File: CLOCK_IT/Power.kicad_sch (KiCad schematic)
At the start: 50 parts, among them Q1 AO3400A, Q2 AO3400A, SW1 CK_KMS2xxG, U10 DS1307ZN_, U4 AXP2101, U5 MC-264, Y2 ABS07-32.768KHZ-T

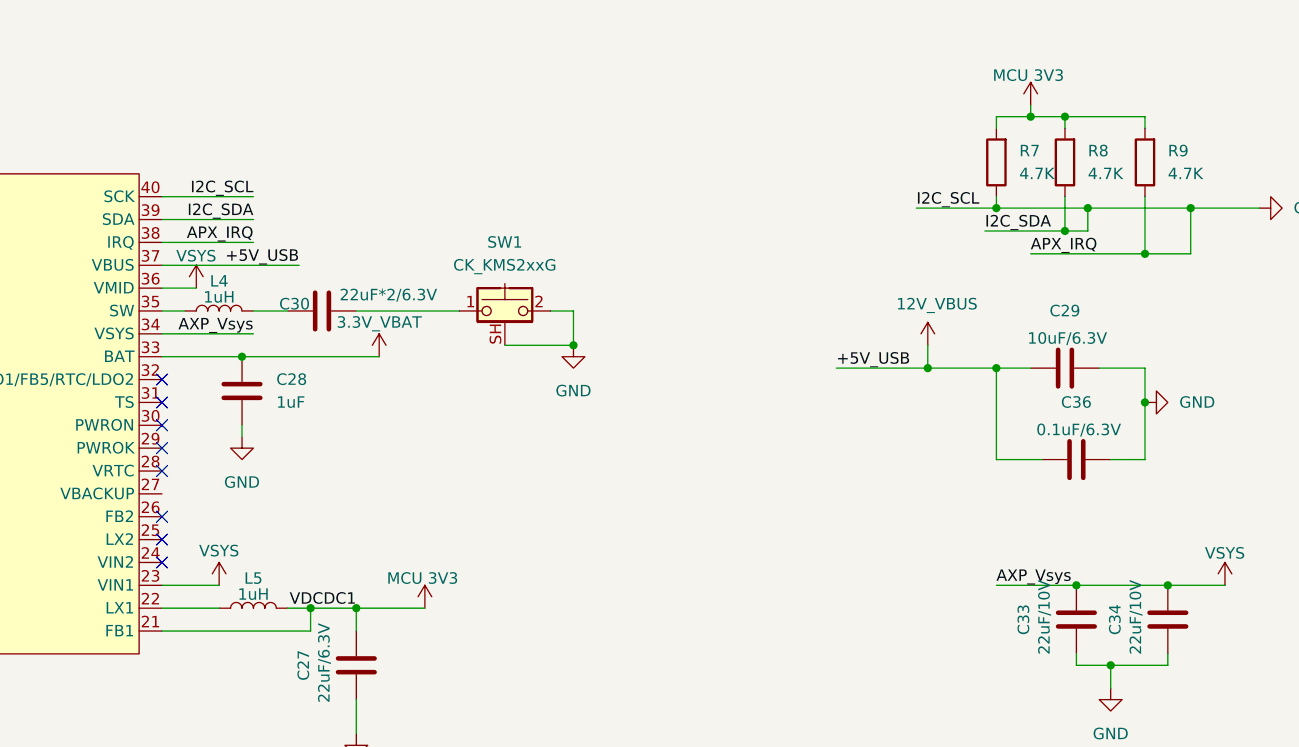
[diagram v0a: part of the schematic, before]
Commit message: :art: small Rereading errors for axp21010 Part 2
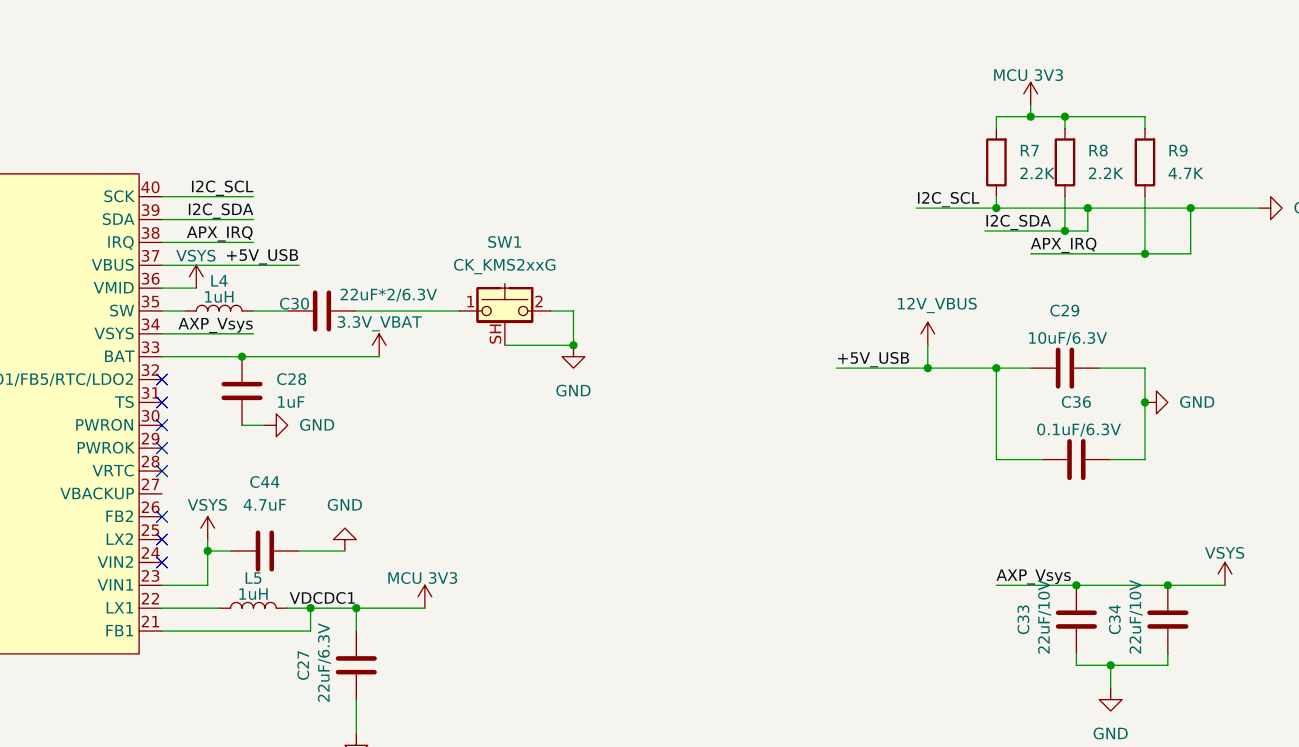
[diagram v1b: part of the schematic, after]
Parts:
- added C44: 4.7uF, symbol Device:C
- R7, R8: value 4.7K -> 2.2K
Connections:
- net GND: now also C44.2
- net VSYS: now also C44.1
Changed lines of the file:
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@@
 	)
 	(junction
+		(at 201.93 78.74)
+		(diameter 0)
+		(color 0 0 0 0)
+	)
+	(junction
 		(at 289.56 58.42)
 		(diameter 0)
@@
 	(wire
 		(pts
+			(xy 201.93 77.47) (xy 201.93 78.74)
+		)
+		(stroke
+			(width 0)
+			(type default)
+		)
+	)
+	(wire
+		(pts
 			(xy 115.57 201.93) (xy 120.65 201.93)
 		)
@@
 	(wire
 		(pts
-			(xy 205.74 64.77) (xy 205.74 66.04)
+			(xy 234.95 55.88) (xy 242.57 55.88)
 		)
 		(stroke
@@
 	(wire
 		(pts
-			(xy 234.95 55.88) (xy 242.57 55.88)
+			(xy 306.07 62.23) (xy 306.07 58.42)
 		)
 		(stroke
@@
 	(wire
 		(pts
-			(xy 306.07 62.23) (xy 306.07 58.42)
+			(xy 124.46 87.63) (xy 133.35 87.63)
 		)
 		(stroke
@@
 	(wire
 		(pts
-			(xy 124.46 87.63) (xy 133.35 87.63)
+			(xy 121.92 52.07) (xy 135.89 52.07)
 		)
 		(stroke
@@
 	(wire
 		(pts
-			(xy 121.92 52.07) (xy 135.89 52.07)
+			(xy 134.62 49.53) (xy 138.43 49.53)
 		)
 		(stroke
@@
 	(wire
 		(pts
-			(xy 134.62 49.53) (xy 138.43 49.53)
+			(xy 201.93 78.74) (xy 204.47 78.74)
 		)
 		(stroke
@@
 	(wire
 		(pts
+			(xy 201.93 78.74) (xy 201.93 82.55)
+		)
+		(stroke
+			(width 0)
+			(type default)
+		)
+	)
+	(wire
+		(pts
 			(xy 138.43 44.45) (xy 120.65 44.45)
 		)
@@
 	(wire
 		(pts
+			(xy 212.09 78.74) (xy 217.17 78.74)
+		)
+		(stroke
+			(width 0)
+			(type default)
+		)
+	)
+	(wire
+		(pts
 			(xy 119.38 38.1) (xy 119.38 35.56)
 		)
@@
 	(wire
 		(pts
+			(xy 208.28 64.77) (xy 205.74 64.77)
+		)
+		(stroke
+			(width 0)
+			(type default)
+		)
+	)
+	(wire
+		(pts
 			(xy 288.29 43.18) (xy 297.18 43.18)
 		)
@@
 	(wire
 		(pts
+			(xy 201.93 82.55) (xy 196.85 82.55)
+		)
+		(stroke
+			(width 0)
+			(type default)
+		)
+	)
+	(wire
+		(pts
 			(xy 35.56 40.64) (xy 35.56 45.72)
 		)
@@
 	(wire
 		(pts
-			(xy 196.85 82.55) (xy 203.2 82.55)
-		)
-		(stroke
-			(width 0)
-			(type default)
-		)
-	)
-	(wire
-		(pts
 			(xy 289.56 68.58) (xy 289.56 58.42)
 		)
@@
 	(symbol
 		(lib_id "power:GND")
-		(at 205.74 66.04 0)
+		(at 208.28 64.77 90)
 		(unit 1)
 		(exclude_from_sim no)
@@
 		(fields_autoplaced yes)
 		(property "Reference" "#PWR071"
-			(at 205.74 72.39 0)
+			(at 214.63 64.77 0)
 			(effects
 				(font
@@
 		)
 		(property "Value" "GND"
-			(at 205.74 71.12 0)
+			(at 212.09 64.7699 90)
 			(effects
 				(font
 					(size 1.27 1.27)
 				)
+				(justify right)
 			)
 		)
 		(property "Footprint" ""
-			(at 205.74 66.04 0)
+			(at 208.28 64.77 0)
 			(effects
 				(font
@@
 		)
 		(property "Datasheet" ""
-			(at 205.74 66.04 0)
+			(at 208.28 64.77 0)
 			(effects
 				(font
@@
 		)
 		(property "Description" "Power symbol creates a global label with name \"GND\" , ground"
-			(at 205.74 66.04 0)
+			(at 208.28 64.77 0)
 			(effects
 				(font
@@
 	(symbol
 		(lib_id "power:+3.3V")
-		(at 203.2 82.55 0)
+		(at 201.93 77.47 0)
 		(unit 1)
 		(exclude_from_sim no)
@@
 		(dnp no)
 		(property "Reference" "#PWR047"
-			(at 203.2 86.36 0)
+			(at 201.93 81.28 0)
 			(effects
 				(font
@@
 		)
 		(property "Value" "VSYS"
-			(at 203.2 78.74 0)
+			(at 201.93 73.66 0)
 			(effects
 				(font
@@
 		)
 		(property "Footprint" ""
-			(at 203.2 82.55 0)
+			(at 201.93 77.47 0)
 			(effects
 				(font
@@
 		)
 		(property "Datasheet" ""
-			(at 203.2 82.55 0)
+			(at 201.93 77.47 0)
 			(effects
 				(font
@@
 		)
 		(property "Description" "Power symbol creates a global label with name \"+3.3V\""
-			(at 203.2 82.55 0)
+			(at 201.93 77.47 0)
 			(effects
 				(font
@@
 	)
 	(symbol
+		(lib_id "Device:C")
+		(at 208.28 78.74 90)
+		(unit 1)
+		(exclude_from_sim no)
+		(in_bom yes)
+		(on_board yes)
+		(dnp no)
+		(fields_autoplaced yes)
+		(property "Reference" "C44"
+			(at 208.28 71.12 90)
+			(effects
+				(font
+					(size 1.27 1.27)
+				)
+			)
+		)
+		(property "Value" "4.7uF"
+			(at 208.28 73.66 90)
+			(effects
+				(font
+					(size 1.27 1.27)
+				)
+			)
+		)
+		(property "Footprint" ""
+			(at 212.09 77.7748 0)
+			(effects
+				(font
+					(size 1.27 1.27)
+				)
+				(hide yes)
+			)
+		)
+		(property "Datasheet" "~"
+			(at 208.28 78.74 0)
+			(effects
+				(font
+					(size 1.27 1.27)
+				)
+				(hide yes)
+			)
+		)
+		(property "Description" "Unpolarized capacitor"
+			(at 208.28 78.74 0)
+			(effects
+				(font
+					(size 1.27 1.27)
+				)
+				(hide yes)
+			)
+		)
+		(pin "2"
+		)
+		(pin "1"
+		)
+		(instances
+			(project "CLOCK_IT"
+				(path "/6c8f4e2a-0be1-4eb1-92e1-07339040f4c9/89057fe9-a1d2-4b06-95ab-71c40c05c07f"
+					(reference "C44")
+					(unit 1)
+				)
+			)
+		)
+	)
+	(symbol
 		(lib_id "Device:R")
 		(at 297.18 35.56 180)
@@
 			)
 		)
-		(property "Value" "4.7K"
+		(property "Value" "2.2K"
 			(at 299.72 36.8299 0)
 			(effects
@@
 			)
 		)
-		(property "Value" "4.7K"
+		(property "Value" "2.2K"
 			(at 292.1 36.8299 0)
 			(effects
@@
 					(unit 1)
 				)
+			)
+		)
+	)
+	(symbol
+		(lib_id "power:GND")
+		(at 217.17 78.74 180)
+		(unit 1)
+		(exclude_from_sim no)
+		(in_bom yes)
+		(on_board yes)
+		(dnp no)
+		(fields_autoplaced yes)
+		(property "Reference" "#PWR077"
+			(at 217.17 72.39 0)
+			(effects
+				(font
+					(size 1.27 1.27)
+				)
+				(hide yes)
+			)
+		)
+		(property "Value" "GND"
+			(at 217.17 73.66 0)
+			(effects
+				(font
+					(size 1.27 1.27)
+				)
+			)
+		)
+		(property "Footprint" ""
+			(at 217.17 78.74 0)
+			(effects
+				(font
+					(size 1.27 1.27)
+				)
+				(hide yes)
+			)
+		)
+		(property "Datasheet" ""
+			(at 217.17 78.74 0)
+			(effects
+				(font
+					(size 1.27 1.27)
+				)
+				(hide yes)
+			)
+		)
+		(property "Description" "Power symbol creates a global label with name \"GND\" , ground"
+			(at 217.17 78.74 0)
+			(effects
+				(font
+					(size 1.27 1.27)
+				)
+				(hide yes)
+			)
+		)
+		(pin "1"
+		)
+		(instances
+			(project "CLOCK_IT"
+				(path "/6c8f4e2a-0be1-4eb1-92e1-07339040f4c9/89057fe9-a1d2-4b06-95ab-71c40c05c07f"
+					(reference "#PWR077")
+					(unit 1)
+				)

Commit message: :art: small Rereading errors for axp21010 Part 3
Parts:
- C25: value 1uF/6.3V -> 1uF
- R6: value 330R -> 470R
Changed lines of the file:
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@@
 			)
 		)
-		(property "Value" "1uF/6.3V"
-			(at 121.412 40.64 90)
+		(property "Value" "1uF"
+			(at 123.952 40.64 90)
 			(effects
 				(font
@@
 			)
 		)
-		(property "Value" "330R"
+		(property "Value" "470R"
 			(at 132.08 34.29 90)
 			(effects

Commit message: :construction:Added RTC connection
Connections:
- net GND: now also C37.2, C38.2, U10.4 (GND)
- net SCL5V: now also U10.6 (SCL)
- net SDA5V: now also U10.5 (SDA)
- net VBAT: now also U10.3 (VBAT)
- net VCC: now also U10.8 (VCC)
- net at C38.1: now also U10.1 (X1), Y2.2
- net at Y2.1: now also C37.1, U10.2 (X2)
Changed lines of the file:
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@@
+	)
+	(junction
+		(at 243.84 207.01)
+		(diameter 0)
+		(color 0 0 0 0)
 	)
 	(junction
@@
 	)
 	(junction
+		(at 227.33 193.04)
+		(diameter 0)
+		(color 0 0 0 0)
+	)
+	(junction
 		(at 306.07 45.72)
 		(diameter 0)
@@
 	)
 	(junction
+		(at 227.33 207.01)
+		(diameter 0)
+		(color 0 0 0 0)
+	)
+	(junction
 		(at 120.65 41.91)
 		(diameter 0)
@@
 	(wire
 		(pts
+			(xy 243.84 193.04) (xy 227.33 193.04)
+		)
+		(stroke
+			(width 0)
+			(type default)
+		)
+	)
+	(wire
+		(pts
 			(xy 240.03 52.07) (xy 242.57 52.07)
 		)
@@
 	(wire
 		(pts
+			(xy 227.33 189.23) (xy 227.33 193.04)
+		)
+		(stroke
+			(width 0)
+			(type default)
+		)
+	)
+	(wire
+		(pts
 			(xy 308.61 91.44) (xy 302.26 91.44)
 		)
@@
 	(wire
 		(pts
+			(xy 289.56 217.17) (xy 289.56 219.71)
+		)
+		(stroke
+			(width 0)
+			(type default)
+		)
+	)
+	(wire
+		(pts
 			(xy 306.07 31.75) (xy 306.07 30.48)
 		)
@@
 	(wire
 		(pts
+			(xy 289.56 199.39) (xy 294.64 199.39)
+		)
+		(stroke
+			(width 0)
+			(type default)
+		)
+	)
+	(wire
+		(pts
 			(xy 271.78 58.42) (xy 281.94 58.42)
 		)
@@
 	(wire
 		(pts
+			(xy 227.33 207.01) (xy 231.14 207.01)
+		)
+		(stroke
+			(width 0)
+			(type default)
+		)
+	)
+	(wire
+		(pts
 			(xy 297.18 43.18) (xy 299.72 43.18)
 		)
@@
 	(wire
 		(pts
+			(xy 250.19 214.63) (xy 259.08 214.63)
+		)
+		(stroke
+			(width 0)
+			(type default)
+		)
+	)
+	(wire
+		(pts
 			(xy 53.34 196.85) (xy 53.34 193.04)
 		)
@@
 	(wire
 		(pts
+			(xy 295.91 207.01) (xy 295.91 228.6)
+		)
+		(stroke
+			(width 0)
+			(type default)
+		)
+	)
+	(wire
+		(pts
 			(xy 115.57 190.5) (xy 124.46 190.5)
 		)
@@
 	(wire
 		(pts
+			(xy 243.84 196.85) (xy 243.84 193.04)
+		)
+		(stroke
+			(width 0)
+			(type default)
+		)
+	)
+	(wire
+		(pts
 			(xy 289.56 58.42) (xy 293.37 58.42)
 		)
@@
 	(wire
 		(pts
+			(xy 300.99 201.93) (xy 289.56 201.93)
+		)
+		(stroke
+			(width 0)
+			(type default)
+		)
+	)
+	(wire
+		(pts
 			(xy 72.39 175.26) (xy 72.39 182.88)
 		)
@@
 	(wire
 		(pts
+			(xy 295.91 228.6) (xy 227.33 228.6)
+		)
+		(stroke
+			(width 0)
+			(type default)
+		)
+	)
+	(wire
+		(pts
 			(xy 124.46 87.63) (xy 133.35 87.63)
 		)
@@
 	(wire
 		(pts
+			(xy 227.33 207.01) (xy 227.33 204.47)
+		)
+		(stroke
+			(width 0)
+			(type default)
+		)
+	)
+	(wire
+		(pts
 			(xy 196.85 49.53) (xy 200.66 49.53)
 		)
@@
 	(wire
 		(pts
+			(xy 243.84 207.01) (xy 259.08 207.01)
+		)
+		(stroke
+			(width 0)
+			(type default)
+		)
+	)
+	(wire
+		(pts
 			(xy 297.18 30.48) (xy 297.18 31.75)
 		)
@@
 	(wire
 		(pts
+			(xy 250.19 201.93) (xy 259.08 201.93)
+		)
+		(stroke
+			(width 0)
+			(type default)
+		)
+	)
+	(wire
+		(pts
 			(xy 100.33 87.63) (xy 100.33 82.55)
 		)
@@
 	(wire
 		(pts
+			(xy 238.76 207.01) (xy 243.84 207.01)
+		)
+		(stroke
+			(width 0)
+			(type default)
+		)
+	)
+	(wire
+		(pts
 			(xy 135.89 52.07) (xy 138.43 52.07)
 		)
@@
 	(wire
 		(pts
+			(xy 227.33 228.6) (xy 227.33 207.01)
+		)
+		(stroke
+			(width 0)
+			(type default)
+		)
+	)
+	(wire
+		(pts
 			(xy 196.85 44.45) (xy 207.01 44.45)
 		)
@@
 	(wire
 		(pts
+			(xy 243.84 204.47) (xy 243.84 207.01)
+		)
+		(stroke
+			(width 0)
+			(type default)
+		)
+	)
+	(wire
+		(pts
 			(xy 137.16 39.37) (xy 137.16 38.1)
 		)
@@
 	(wire
 		(pts
+			(xy 300.99 196.85) (xy 300.99 201.93)
+		)
+		(stroke
+			(width 0)
+			(type default)
+		)
+	)
+	(wire
+		(pts
+			(xy 227.33 193.04) (xy 227.33 196.85)
+		)
+		(stroke
+			(width 0)
+			(type default)
+		)
+	)
+	(wire
+		(pts
 			(xy 101.6 203.2) (xy 106.68 203.2)
 		)
@@
 		)
 		(stroke
+			(width 0)
+			(type default)
+		)
+	)
+	(wire
+		(pts
+			(xy 294.64 199.39) (xy 294.64 194.31)
+		)
+		(stroke
+			(width 0)
+			(type default)
+		)
+	)
+	(wire
+		(pts
+			(xy 289.56 207.01) (xy 295.91 207.01)
+		)
+		(stroke

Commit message: :construction:Added RTC connection unstipulated
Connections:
- net 3V3: now also C37.1, C38.1, D9.2 (A), R60.1, R61.1, R63.1, R64.1
- net GND: now also BT1.2, C37.2, C38.2
- net IIC_SCL: now also Q2.2 (S), R64.2
- net IIC_SDA: now also Q1.2 (S), R61.2
- net SCL5V: now also Q2.3 (D), R62.2
- net SDA5V: now also Q1.3 (D), R59.2
- net VBAT: now also D10.1 (K), D9.1 (K)
- net VCC: now also R59.1, R62.1
- net at Q1.1 (G): now also R60.2
- net at D10.2 (A): now also BT1.1, BT1.S+2
- net at Q2.1 (G): now also R63.2

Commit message: :construction:Added RTC connection unstipulated
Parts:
- renumbered C38 to C100, C37 to C101, C38 to C102, C37 to C103
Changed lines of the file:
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@@
 		(dnp no)
 		(fields_autoplaced yes)
-		(property "Reference" "C37"
+		(property "Reference" "C101"
 			(at 345.44 212.0899 0)
 			(effects
@@
 			(project "CLOCK_IT"
 				(path "/6c8f4e2a-0be1-4eb1-92e1-07339040f4c9/89057fe9-a1d2-4b06-95ab-71c40c05c07f"
-					(reference "C37")
+					(reference "C101")
 					(unit 1)
 				)
@@
 		(on_board yes)
 		(dnp no)
-		(fields_autoplaced yes)
-		(property "Reference" "C38"
-			(at 327.66 212.0899 0)
+		(property "Reference" "C100"
+			(at 327.66 212.09 0)
 			(effects
 				(font
@@
 			(project "CLOCK_IT"
 				(path "/6c8f4e2a-0be1-4eb1-92e1-07339040f4c9/89057fe9-a1d2-4b06-95ab-71c40c05c07f"
-					(reference "C38")
+					(reference "C100")
 					(unit 1)
 				)
@@
 		(dnp no)
 		(fields_autoplaced yes)
-		(property "Reference" "C38"
-			(at 240.03 201.9301 0)
+		(property "Reference" "C102"
+			(at 247.65 199.3899 0)
 			(effects
 				(font
 					(size 1.27 1.27)
 				)
-				(justify left)
+				(justify right)
 			)
 		)
 		(property "Value" "12pF"
-			(at 240.03 199.3901 0)
+			(at 247.65 201.9299 0)
 			(effects
 				(font
 					(size 1.27 1.27)
 				)
-				(justify left)
+				(justify right)
 			)
 		)
@@
 			(project "CLOCK_IT"
 				(path "/6c8f4e2a-0be1-4eb1-92e1-07339040f4c9/89057fe9-a1d2-4b06-95ab-71c40c05c07f"
-					(reference "C38")
+					(reference "C102")
 					(unit 1)
 				)
@@
 		(dnp no)
 		(fields_autoplaced yes)
-		(property "Reference" "C37"
-			(at 223.52 201.9301 0)
+		(property "Reference" "C103"
+			(at 231.14 199.3899 0)
 			(effects
 				(font
 					(size 1.27 1.27)
 				)
-				(justify left)
+				(justify right)
 			)
 		)
 		(property "Value" "12pF"
-			(at 223.52 199.3901 0)
+			(at 231.14 201.9299 0)
 			(effects
 				(font
 					(size 1.27 1.27)
 				)
-				(justify left)
+				(justify right)
 			)
 		)
@@
 			(project "CLOCK_IT"
 				(path "/6c8f4e2a-0be1-4eb1-92e1-07339040f4c9/89057fe9-a1d2-4b06-95ab-71c40c05c07f"
-					(reference "C37")
+					(reference "C103")
 					(unit 1)
 				)

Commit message: :fire:changed the rtc to a 3.3v one
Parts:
- removed U10: DS1307ZN_, DS1307ZN_:SOIC127P600X175-8N, symbol DS1307ZN_:DS1307ZN_
- added U6: DS1338Z-NF, easyeda2kicad:SOP-8_L4.9-W3.9-P1.27-LS6.0-BL, symbol DS1338Z-NF:DS1338Z-NF
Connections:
- net VCC is gone; now on net MCU 3V3: R59.1, R62.1
- net GND: now also U6.4 (GND)
- net MCU 3V3: now also U6.8 (VCC)
- net VBAT: now also U6.3 (VBAT)
- net at C102.1, Y2.2: now also U6.1 (X1)
- net at C103.1, Y2.1: now also U6.2 (X2)
- new net SCL_0.3V: U6.6 (SC)
- new net SDA_0.3V: U6.5 (SDA)
- no-connect marks 26 -> 25
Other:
- moved on the sheet: C102, C103, Y2

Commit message: :white_check_mark: Halffway here
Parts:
- removed BT1: BK-5058, BK-5058:BAT_BK-5058, symbol BK-5058:BK-5058
- removed C100: 100nF 50V, Capacitor_SMD:C_0201_0603Metric, symbol Device:C
- removed C101: 10uF 10V, Capacitor_SMD:C_0201_0603Metric, symbol Device:C
- removed D10, D9: 1N4148W, Diode_SMD:D_SOD-123, symbol Diode:1N4148W
- removed Q1, Q2: AO3400A, Package_TO_SOT_SMD:SOT-23, symbol Transistor_FET:AO3400A
- removed R59, R60, R61, R62, R63, R64: 475, Resistor_SMD:R_01005_0402Metric, symbol Device:R_US
